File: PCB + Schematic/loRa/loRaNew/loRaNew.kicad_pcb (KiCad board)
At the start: 2 copper layers, 3 x 3 mm, 12 parts, among them J1 Left, J2 Right, J3 GPS, J4 MPU-9250, J7 OLED, SW1 SW_SPDT, U1 ESP32-DEVKIT-V1

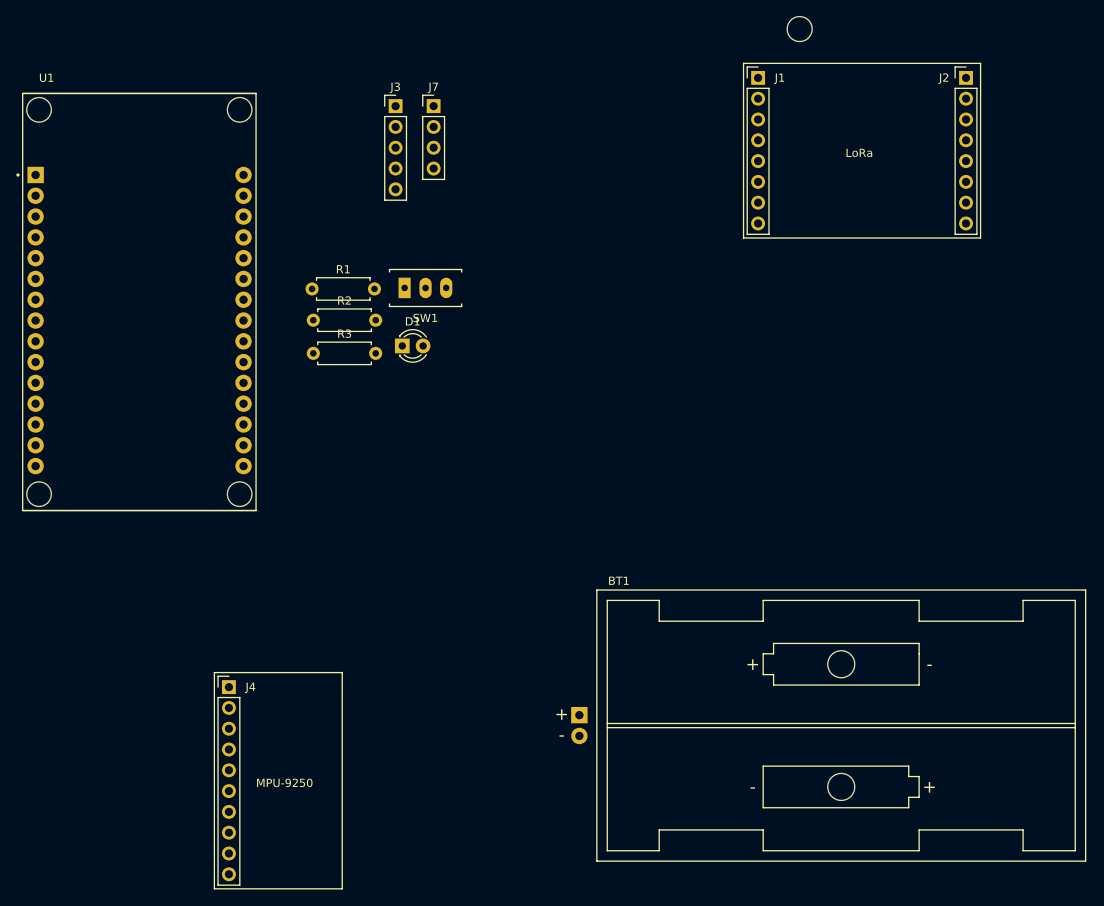
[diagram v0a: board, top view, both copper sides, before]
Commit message: LoRa PCB
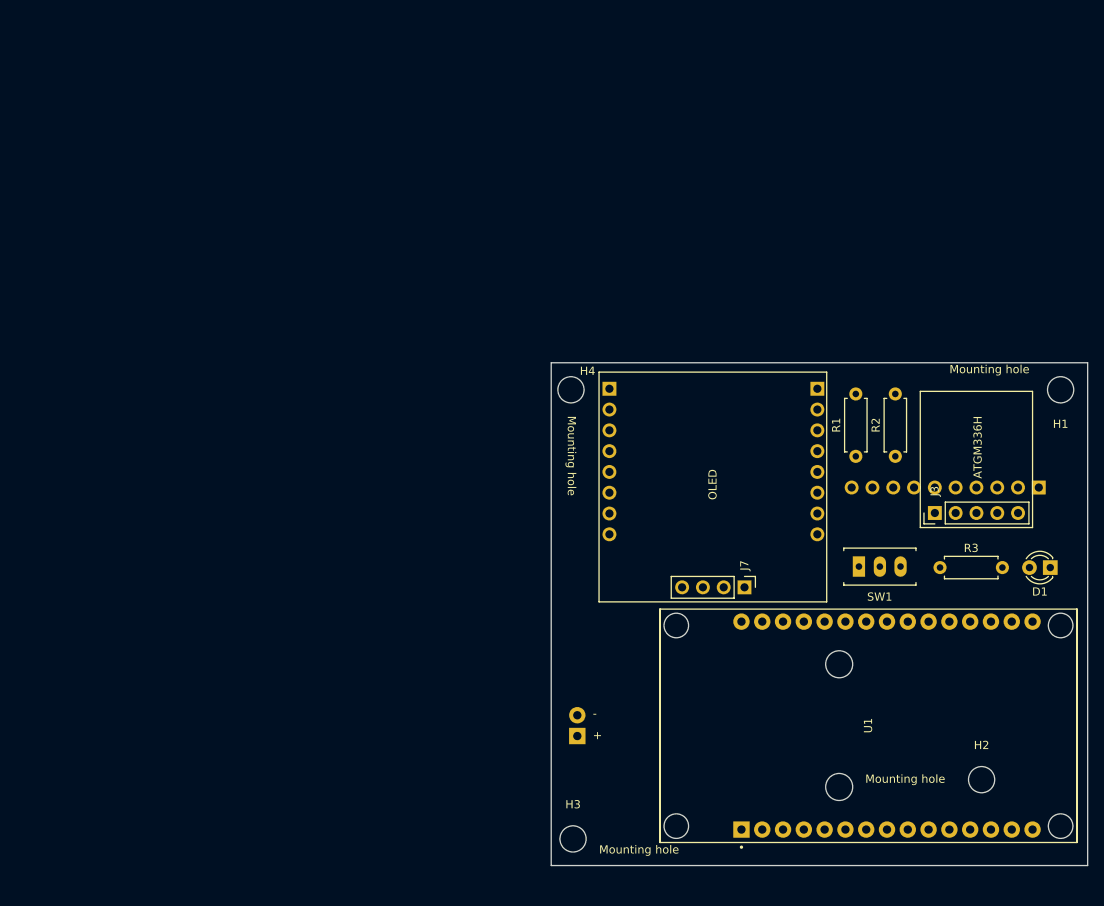
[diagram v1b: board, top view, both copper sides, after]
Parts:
- added H1: MountingHole, MountingHole:MountingHole_3.2mm_M3, F.Cu at (247.8, 84.7)
- added H2: MountingHole, MountingHole:MountingHole_3.2mm_M3, F.Cu at (238.1, 132.3)
- added H3: MountingHole, MountingHole:MountingHole_3.2mm_M3, F.Cu at (188.2, 139.6)
- added H4: MountingHole, MountingHole:MountingHole_3.2mm_M3, F.Cu at (188.0, 84.7)
- BT1, J1, J2, J4: moved to B.Cu
- moved U1 103.0 mm to (224.3, 125.7), turned to 90 degrees
- moved J4 101.9 mm to (245.1, 96.6), turned to 90 degrees
- moved D1 83.7 mm to (246.5, 106.4), turned to 180 degrees
- moved J3 82.5 mm to (232.4, 99.8), turned to 90 degrees
- moved R3 80.9 mm to (233.0, 106.4)
- moved R2 73.0 mm to (227.6, 92.8), turned to 90 degrees
- moved J7 70.0 mm to (209.2, 108.8), turned to -90 degrees
- moved R1 69.5 mm to (222.8, 92.8), turned to 90 degrees
- moved SW1 65.1 mm to (225.7, 106.3)
- moved J2 57.8 mm to (192.7, 84.6), turned to 180 degrees
- moved J1 38.7 mm to (218.1, 84.6), turned to 180 degrees
- moved BT1 15.0 mm to (193.6, 133.2)
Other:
- board size 3 x 3 mm -> 65.5 x 61.4 mm
- board text added: "+"
- board text added: "-"
- board text added: "ATGM336H"
- board text added: "Mounting hole"
- board text added: "OLED"

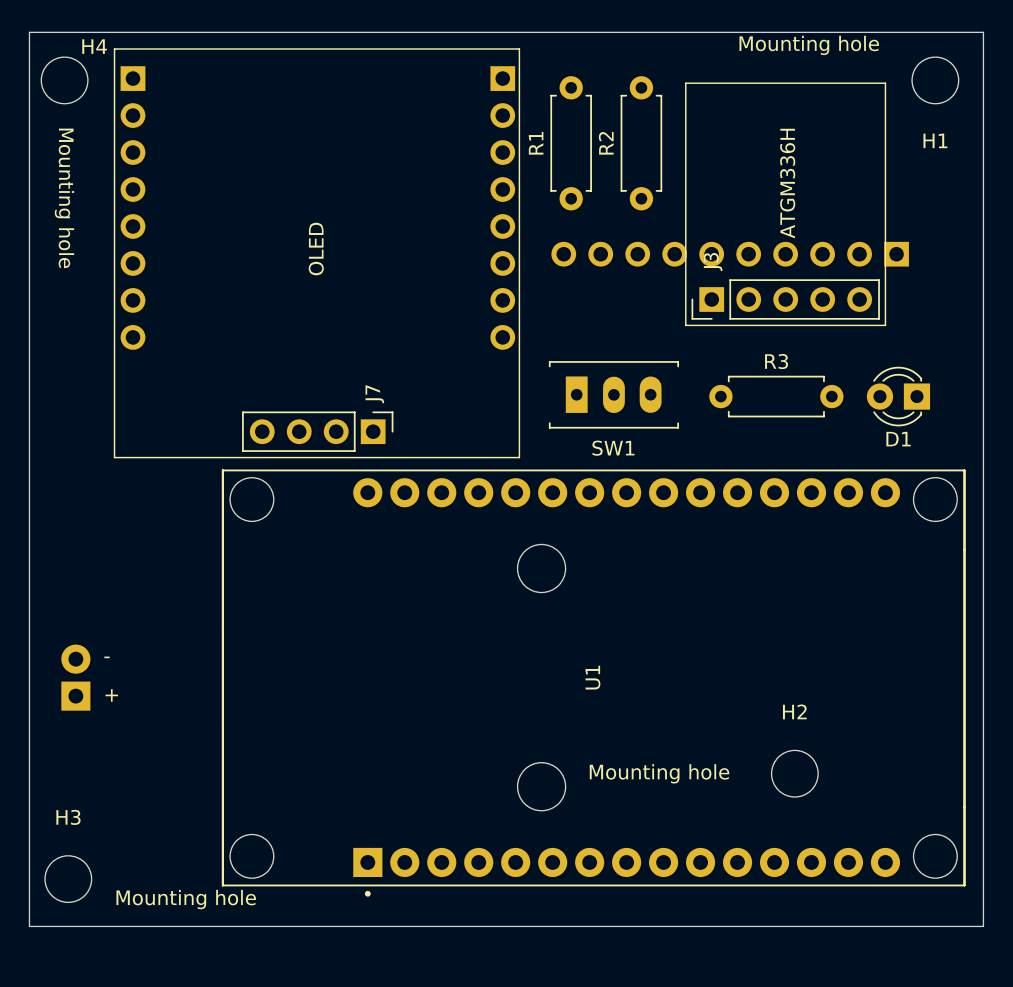
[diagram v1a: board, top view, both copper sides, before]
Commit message: LoRa PCB
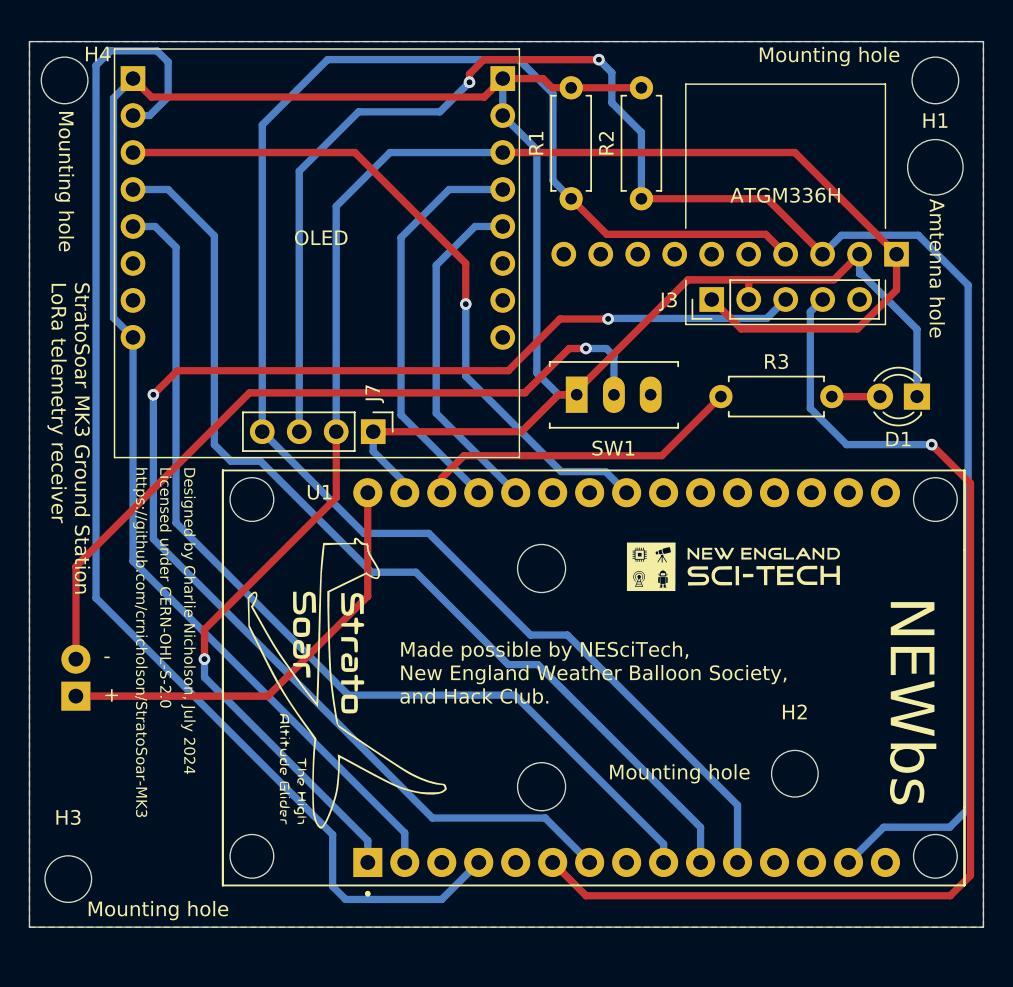
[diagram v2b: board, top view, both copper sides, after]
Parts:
- added G***: LOGO, LOGO, F.Cu at (207.4, 126.1)
- added G***: LOGO, LOGO, F.Cu at (234.1, 118.1)
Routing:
- net GND: track 0.00 -> 180.0 mm
- net SCL: track 0.00 -> 124.4 mm, vias 0 -> 2
- net SDA: track 0.00 -> 115.1 mm
- net +3.3V: track 0.00 -> 113.5 mm, vias 0 -> 1
- net TX: track 0.00 -> 95.2 mm, vias 0 -> 2
- net CS: track 0.00 -> 85.6 mm
- net RX: track 0.00 -> 78.1 mm, vias 0 -> 1
- net MISO: track 0.00 -> 68.0 mm
- net SCK: track 0.00 -> 66.4 mm
- net Net-(BT1--): track 0.00 -> 52.4 mm, vias 0 -> 1
- net MOSI: track 0.00 -> 48.1 mm, vias 0 -> 1
- net +BATT: track 0.00 -> 30.0 mm
- net LORA_RST: track 0.00 -> 28.1 mm
- net DIO0: track 0.00 -> 23.6 mm
- net LED: track 0.00 -> 22.5 mm
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- added copper zone on B.Cu, net GND
- added copper zone on F.Cu, net GND
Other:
- board size 65.5 x 61.4 mm -> 65.5 x 60.8 mm
- board text added: "Amtenna hole"
- board text added: "Designed by Charlie Nicholson, July 2024"
- board text added: "Licensed under CERN-OHL-S-2.0"
- board text added: "Made possible by NESciTech, New England Weather Balloon Society, and Hack Club."
- board text added: "NEWbs"
- board text added: "StratoSoar MK3 Ground Station LoRa telemetry receiver"
- board text added: "https://github.com/crnicholson/StratoSoar-MK3"
